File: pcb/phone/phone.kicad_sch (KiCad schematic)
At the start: 27 parts, among them CN1 S2B-PH-SM4-TB, U4 TPS63021DSJR, U5 TPS7A0218PDBVR, U6 MCP73831-2ACI/MC, U7 MAX17048G+T10

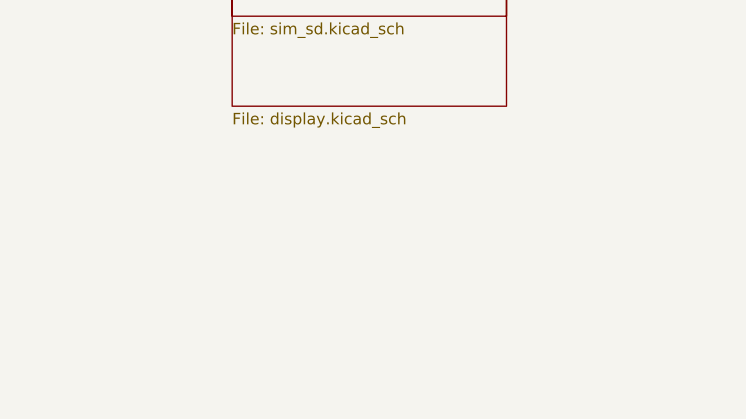
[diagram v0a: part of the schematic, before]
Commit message: Split display sheet into main board + daughterboard
The flip/clamshell design has two PCBs connected via hinge flex. The display
sheet previously contained all display connectors on one sheet, which didn't
match the physical architecture.

Changes:
- display.kicad_sch: Now contains ONLY J_HINGE (hinge flex connector) and
  its associated wires, labels, and power symbols. Title updated to
  "Display (Main Board)".
- display_daughter.kicad_sch (new): Contains J_DISP (main display panel),
  J_DISP2 (outer display panel), J_EARPIECE (earpiece speaker), R14
  (backlight resistor), C37 (decoupling cap), and their associated wires,
  labels, and power symbols. Title: "Display Daughterboard".
- phone.kicad_sch: Added hierarchical sheet instance for Display_Daughter
  at (254, 340), page 6.

Global labels (DISP_MOSI, DISP_SCK, DISP_CS, DISP_DC, DISP_RST, OUTER_CS,
OUTER_DC, BL_PWM, EARPIECE+, EARPIECE-, +3.3V, GND) continue to connect
correctly across sheets via global label connectivity.

ERC result: 274 violations (all pre-existing on root sheet). Display and
Display_Daughter sheets are both ERC-clean.

Generated with [Devin](https://devin.ai)

Co-Authored-By: Devin <158243242+devin-ai-integration[bot]@users.noreply.github.com>
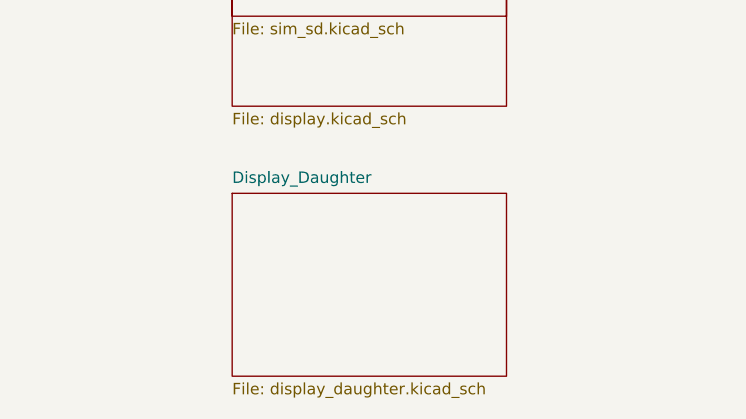
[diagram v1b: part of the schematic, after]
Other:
- added sheet Display_Daughter (display_daughter.kicad_sch)
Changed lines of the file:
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@@
+		)
+	)
+	(sheet
+		(at 254 340)
+		(size 30.48 20.32)
+		(exclude_from_sim no)
+		(in_bom yes)
+		(on_board yes)
+		(dnp no)
+		(fields_autoplaced yes)
+		(stroke
+			(width 0.1524)
+			(type solid)
+		)
+		(fill
+			(color 0 0 0 0)
+		)
+		(property "Sheetname" "Display_Daughter"
+			(at 254 339 0)
+			(show_name no)
+			(do_not_autoplace no)
+			(effects
+				(font
+					(size 1.27 1.27)
+				)
+				(justify left bottom)
+			)
+		)
+		(property "Sheetfile" "display_daughter.kicad_sch"
+			(at 254 361 0)
+			(show_name no)
+			(do_not_autoplace no)
+			(effects
+				(font
+					(size 1.27 1.27)
+				)
+				(justify left top)
+			)
+		)
+		(instances
+			(project "phone"
+				(path "/451c3b43-1616-42cb-bf96-d436f4db82c2"
+					(page "6")
+				)
+			)
 		)
 	)

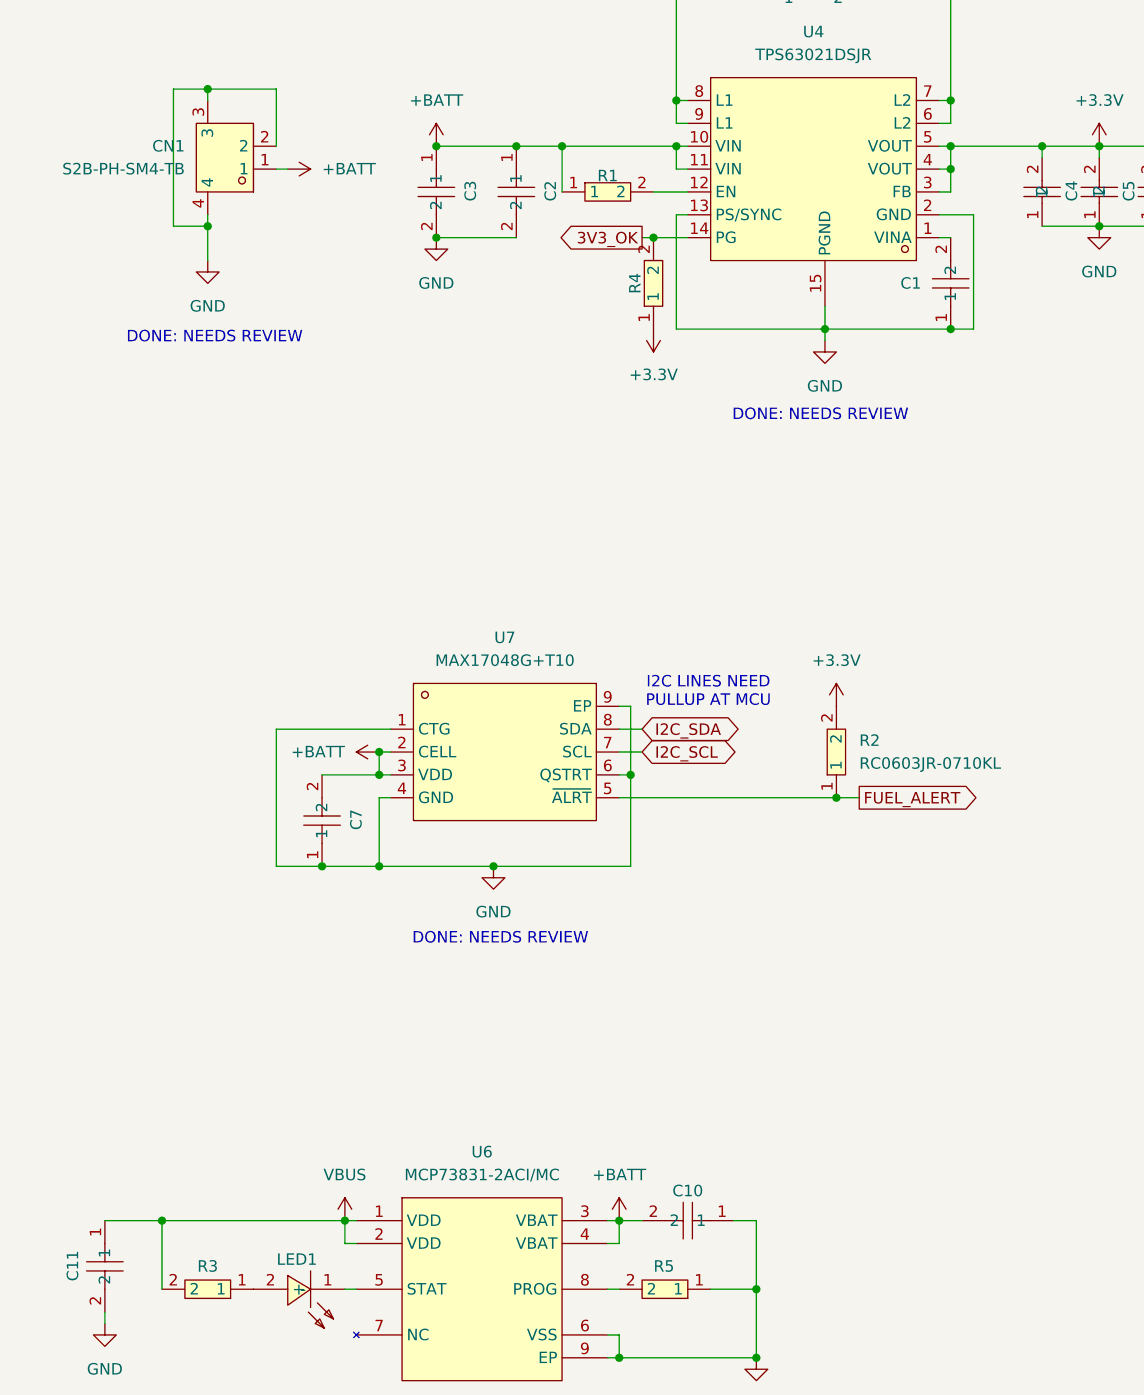
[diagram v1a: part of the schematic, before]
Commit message: Fix root sheet ERC errors: power pins and pin-to-pin conflicts
Fixed all 5 ERC errors on the root sheet (power section):

1. U4 (TPS63021DSJR) Pin 5 (VOUT): Changed from power_out to passive.
   Pin 4 and Pin 5 are both VOUT pins internally connected — having both
   as power_out causes a pin_to_pin conflict. Pin 4 remains power_out
   (drives +3.3V net), Pin 5 is now passive.

2. U6 (MCP73831-2ACI_MC) Pin 4 (VBAT): Changed from power_out to passive.
   Pin 3 and Pin 4 are both VBAT pins internally connected — same issue.
   Pin 3 remains power_out (drives +BATT net), Pin 4 is now passive.

3. U4 Pin 1 (VINA) not driven: Added +BATT power symbol (#PWR024) at
   (119.38, 44.45) connecting to VINA pin. VINA is the analog supply
   input and should be on the same net as VIN (+BATT).

4. GND net not driven: Added PWR_FLAG symbol (#FLG025) at (33.02, 43.18)
   connecting to GND net. PWR_FLAG tells ERC the net is driven by an
   external source.

5. VBUS net not driven: Added PWR_FLAG symbol (#FLG026) at (25.4, 153.67)
   connecting to VBUS net. VBUS comes from USB-C connector (passive pins),
   so PWR_FLAG is needed to tell ERC the net is externally driven.

Result: 0 errors (down from 5). 271 warnings remain (all pre-existing:
227 endpoint_off_grid from non-1.27mm connector pitches, 35
lib_symbol_mismatch from easyeda2kicad, 9 isolated_pin_label).

Generated with [Devin](https://devin.ai)

Co-Authored-By: Devin <158243242+devin-ai-integration[bot]@users.noreply.github.com>
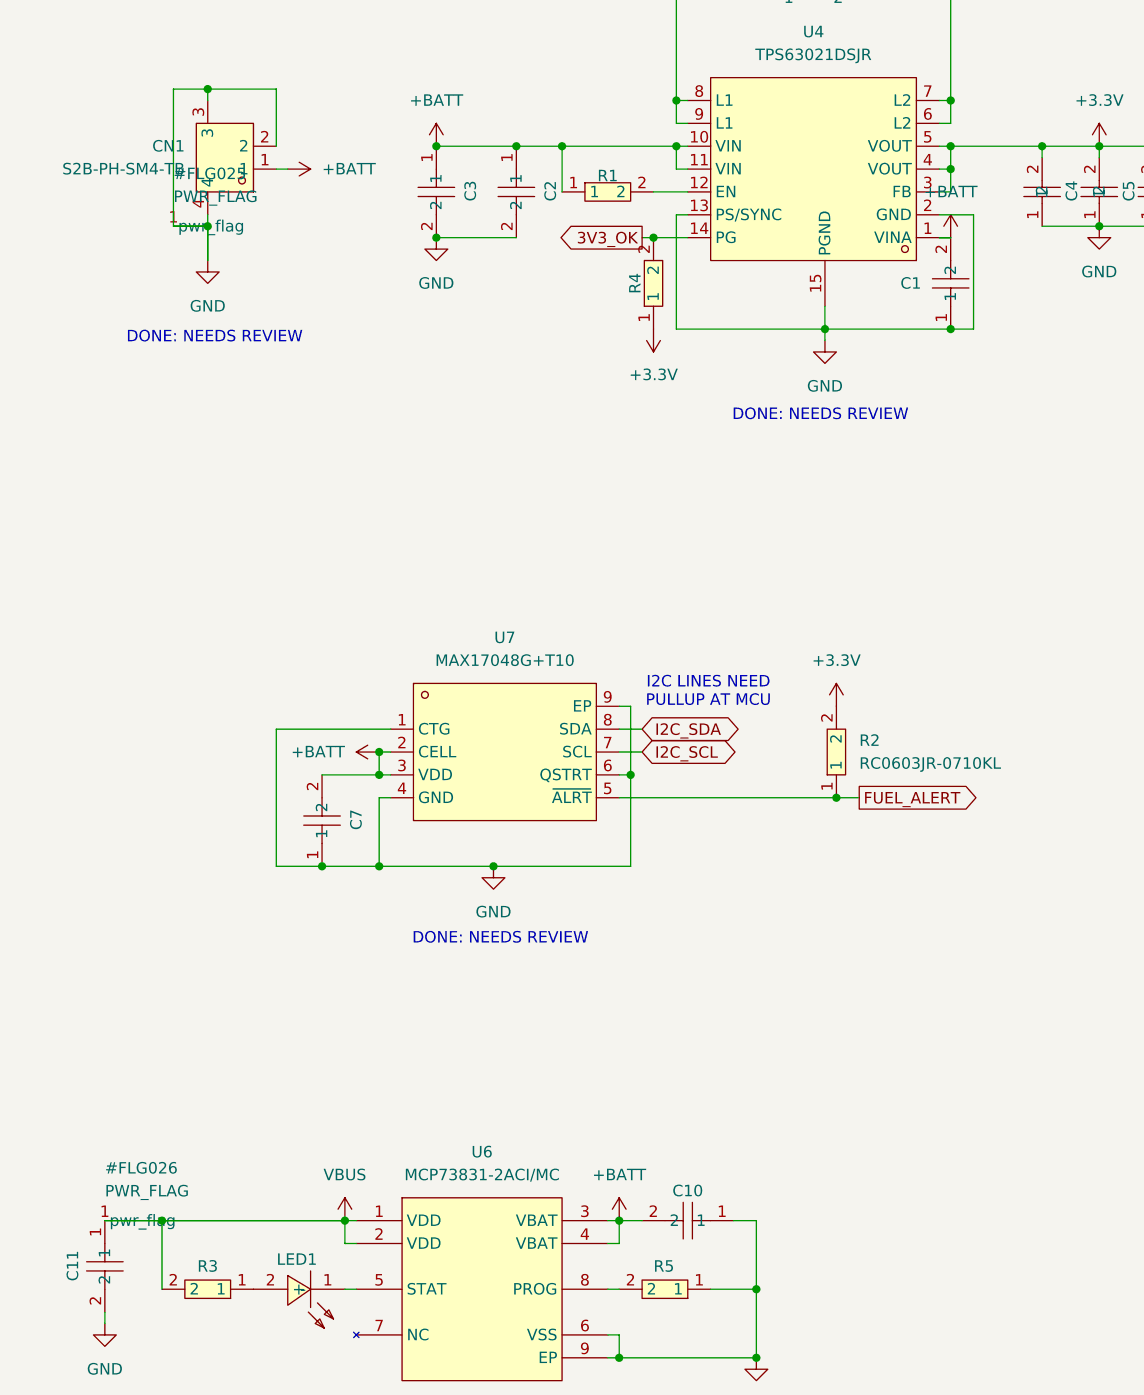
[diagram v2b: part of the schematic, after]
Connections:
- net +BATT: now also C1.2, U4.1 (VINA)
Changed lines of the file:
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@@
 		)
 	)
+		(symbol
+			(lib_id "power:PWR_FLAG")
+			(at 33.02 43.18 0)
+			(unit 1)
+			(body_style 1)
+			(exclude_from_sim no)
+			(in_bom yes)
+			(on_board yes)
+			(in_pos_files yes)
+			(dnp no)
+			(fields_autoplaced yes)
+			(property "Reference" "#FLG025"
+				(at 33.02 38.1 0)
+				(show_name no)
+				(do_not_autoplace no)
+				(effects
+					(font
+						(size 1.27 1.27)
+					)
+					(justify left bottom)
+				)
+			)
+			(property "Value" "PWR_FLAG"
+				(at 33.02 40.64 0)
+				(show_name no)
+				(do_not_autoplace no)
+				(effects
+					(font
+						(size 1.27 1.27)
+					)
+					(justify left bottom)
+				)
+			)
+			(property "Footprint" ""
+				(at 33.02 43.18 0)
+				(show_name no)
+				(do_not_autoplace no)
+				(hide yes)
+				(effects
+					(font
+						(size 1.27 1.27)
+					)
+					(hide yes)
+				)
+			)
+			(property "Datasheet" ""
+				(at 33.02 43.18 0)
+				(show_name no)
+				(do_not_autoplace no)
+				(hide yes)
+				(effects
+					(font
+						(size 1.27 1.27)
+					)
+					(hide yes)
+				)
+			)
+			(instances
+				(project "phone"
+					(path "/451c3b43-1616-42cb-bf96-d436f4db82c2"
+						(reference "#FLG025")
+						(unit 1)
+					)
+				)
+			)
+		)
+		(symbol
+			(lib_id "power:PWR_FLAG")
+			(at 25.4 153.67 0)
+			(unit 1)
+			(body_style 1)
+			(exclude_from_sim no)
+			(in_bom yes)
+			(on_board yes)
+			(in_pos_files yes)
+			(dnp no)
+			(fields_autoplaced yes)
+			(property "Reference" "#FLG026"
+				(at 25.4 148.59 0)
+				(show_name no)
+				(do_not_autoplace no)
+				(effects
+					(font
+						(size 1.27 1.27)
+					)
+					(justify left bottom)
+				)
+			)
+			(property "Value" "PWR_FLAG"
+				(at 25.4 151.13 0)
+				(show_name no)
+				(do_not_autoplace no)
+				(effects
+					(font
+						(size 1.27 1.27)
+					)
+					(justify left bottom)
+				)
+			)
+			(property "Footprint" ""
+				(at 25.4 153.67 0)
+				(show_name no)
+				(do_not_autoplace no)
+				(hide yes)
+				(effects
+					(font
+						(size 1.27 1.27)
+					)
+					(hide yes)
+				)
+			)
+			(property "Datasheet" ""
+				(at 25.4 153.67 0)
+				(show_name no)
+				(do_not_autoplace no)
+				(hide yes)
+				(effects
+					(font
+						(size 1.27 1.27)
+					)
+					(hide yes)
+				)
+			)
+			(instances
+				(project "phone"
+					(path "/451c3b43-1616-42cb-bf96-d436f4db82c2"
+						(reference "#FLG026")
+						(unit 1)
+					)
+				)
+			)
+		)
+		(symbol
+			(lib_id "power:+BATT")
+			(at 119.38 44.45 0)
+			(unit 1)
+			(body_style 1)
+			(exclude_from_sim no)
+			(in_bom yes)
+			(on_board yes)
+			(in_pos_files yes)
+			(dnp no)
+			(fields_autoplaced yes)
+			(property "Reference" "#PWR024"
+				(at 119.38 48.26 0)
+				(hide yes)
+				(show_name no)
+				(do_not_autoplace no)
+				(effects
+					(font
+						(size 1.27 1.27)
+					)
+				)
+			)
+			(property "Value" "+BATT"
+				(at 119.38 39.37 0)
+				(show_name no)
+				(do_not_autoplace no)
+				(effects
+					(font
+						(size 1.27 1.27)
+					)
+				)
+			)
+			(property "Footprint" ""
+				(at 119.38 44.45 0)
+				(hide yes)
+				(show_name no)
+				(do_not_autoplace no)
+				(effects
+					(font
+						(size 1.27 1.27)
+					)
+					(hide yes)
+				)
+			)
+			(property "Datasheet" ""
+				(at 119.38 44.45 0)
+				(show_name no)
+				(do_not_autoplace no)
+				(hide yes)
+				(effects
+					(font
+						(size 1.27 1.27)
+					)
+					(hide yes)
+				)
+			)
+			(instances
+				(project "phone"
+					(path "/451c3b43-1616-42cb-bf96-d436f4db82c2"
+						(reference "#PWR024")
+						(unit 1)
+					)
+				)
+			)
+		)
+		(wire
+			(pts
+				(xy 33.02 43.18) (xy 36.83 43.18)
+			)
+			(stroke
+				(width 0)
+				(type default)
+			)
+		)
+		(wire
+			(pts
+				(xy 36.83 43.18) (xy 36.83 46.99)
+			)
+			(stroke
+				(width 0)
+				(type default)
+			)
+		)
+		(wire
+			(pts
+				(xy 25.4 153.67) (xy 52.07 153.67)
+			)
+			(stroke
+				(width 0)
+				(type default)
+			)
+		)
+		(wire
+			(pts
+				(xy 119.38 44.45) (xy 118.11 44.45)
+			)
+			(stroke
+				(width 0)
+				(type default)
+			)
+		)
 	(sheet_instances
 		(path "/"

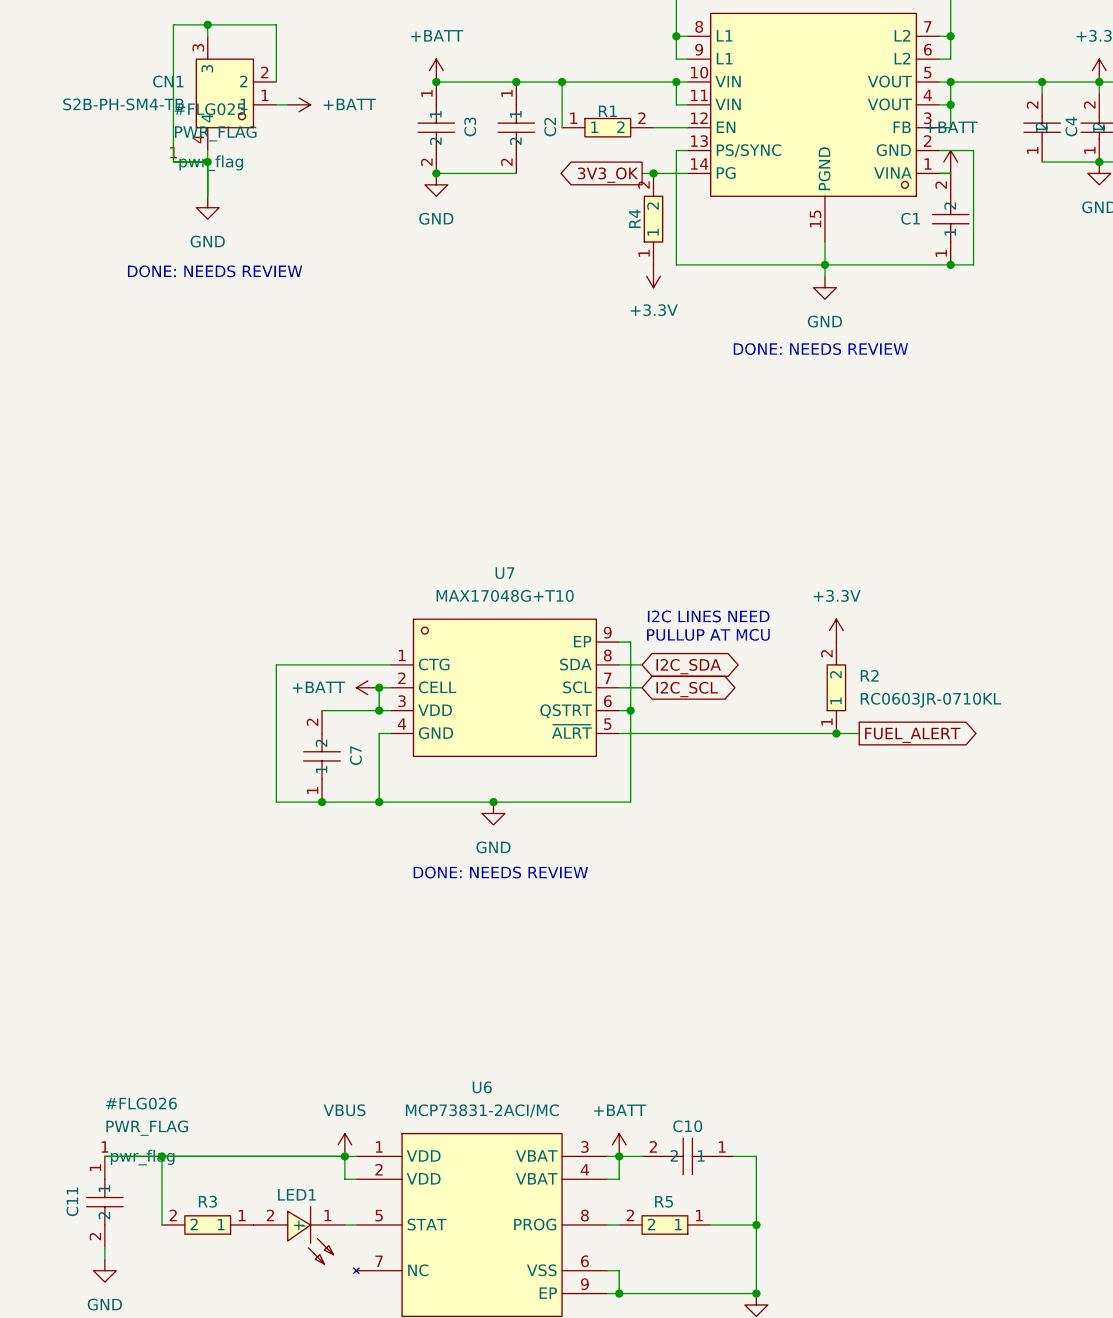
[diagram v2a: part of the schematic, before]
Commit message: User edits: keypad rewiring, sheet reorder, ERC severity reverts, R24 fix
Keypad (keypad.kicad_sch):
- Rotated all 20 switches 270 degrees for vertical contact orientation
- Wired all 4 pins on each switch (pins 1&2 to column, pins 3&4 to row)
- Removed all 37 no_connect markers on pins 3&4
- Cleaned up to 25.4mm (1-inch) grid spacing
- Added pull-down resistors to all 4 columns (was only KEY_COL3)

Root sheet (phone.kicad_sch):
- Reordered sub-sheet blocks (Display_Daughter before SIM_SD)
- Cleaned up PWR_FLAG symbol formatting/indentation
- Reordered PWR_FLAG and +BATT symbol placement

MCU sheet (mcu.kicad_sch):
- Repositioned +3.3V power symbol (#PWR32) at pin 190.5,200.66

Project settings (phone.kicad_pro):
- Reverted ERC suppressions: endpoint_off_grid, isolated_pin_label,
  lib_symbol_mismatch back to warning (want actual fixes, not ignores)
- Added SW2-20 to used designators
- Reordered sheets list (Display_Daughter before SIM_SD)

Other sheets (codec, display, display_daughter, sim_sd):
- KiCad editor reformatting upon save

Generated with [Devin](https://devin.ai)

Co-Authored-By: Devin <158243242+devin-ai-integration[bot]@users.noreply.github.com>
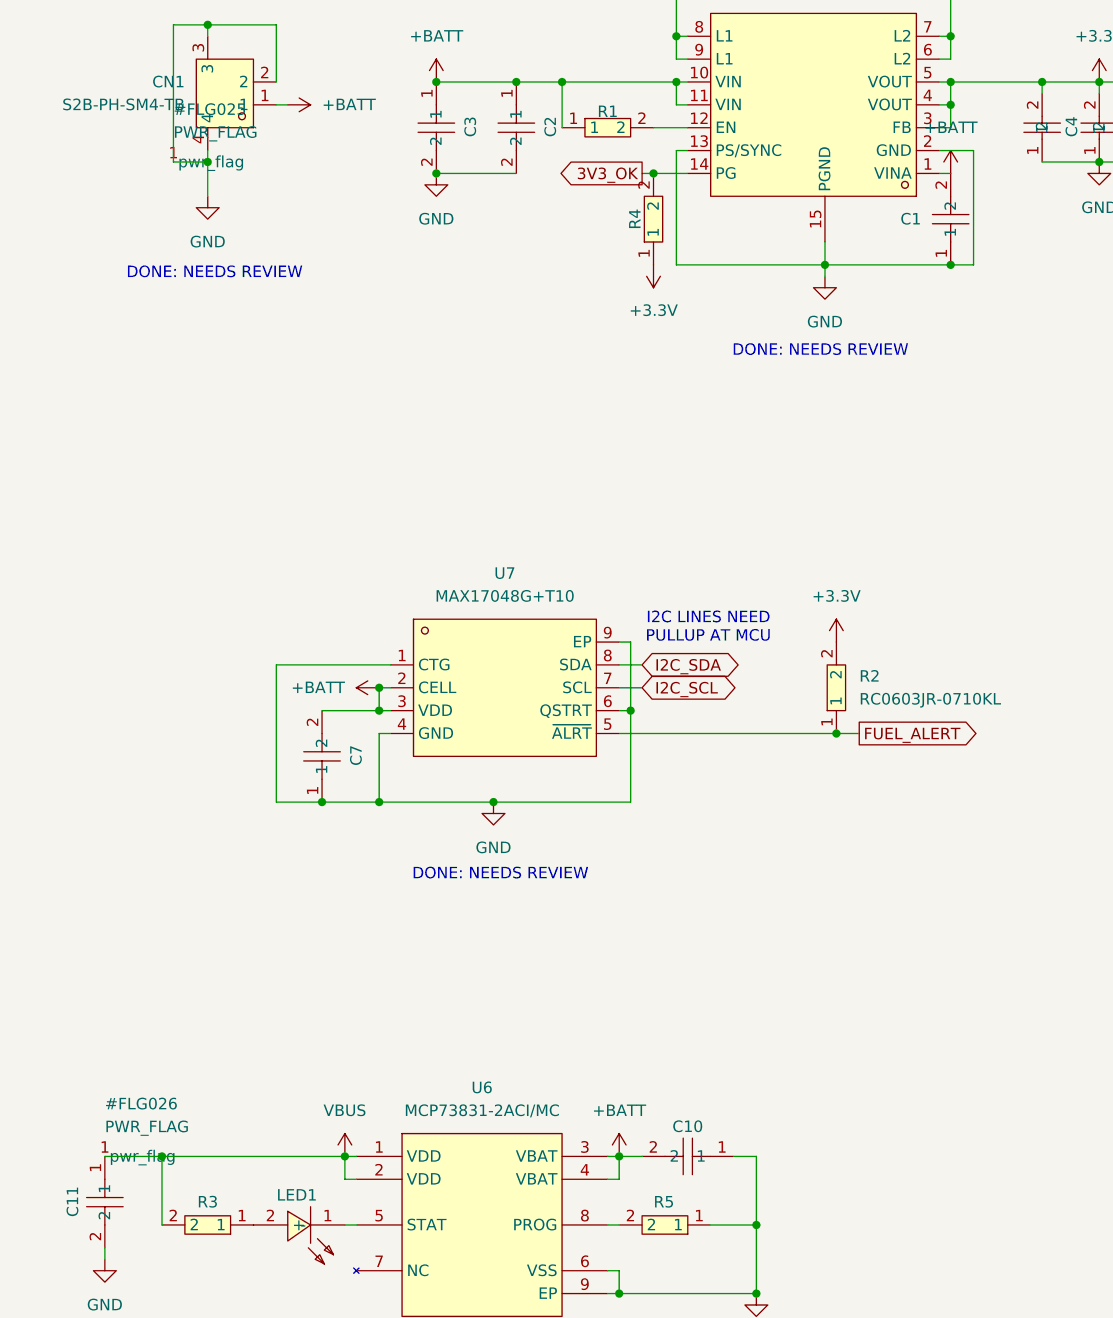
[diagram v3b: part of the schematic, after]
